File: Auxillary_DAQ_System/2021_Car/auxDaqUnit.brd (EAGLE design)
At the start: 130.8 x 114 mm, 39 parts, among them IC1 ADS1119IPWT, IC2 TPS563231DRLR, J1 1990083, J10 1990083, J11 1990083, J12 1990083, J2 1990083, J3 1990083, J4 1990083, J5 1990083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

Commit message: updated schematic and pinout
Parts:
- added C8: 0.1uF, SparkFun-Capacitors:0603
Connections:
- net 14: now also J10.1; no longer J7.8
- net 15: now also J7.1; no longer J10.8
- net 32: now also J7.8; no longer J10.1
- net 33: now also J10.8; no longer J7.1
- net 5V: now also C8.1, IC1.9
- net GND: now also C8.2, IC2.3; no longer IC1.9
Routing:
- net 15: track 269.2 -> 196.0 mm
- net 33: track 146.2 -> 188.5 mm
- net 14: track 214.0 -> 253.9 mm
- net 32: track 145.1 -> 153.7 mm
- net 5V: track 163.6 -> 167.1 mm
- net 17: track 250.9 -> 252.3 mm
- net 16: track 248.9 -> 250.0 mm
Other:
- board text added: "20"
- board text added: "21"

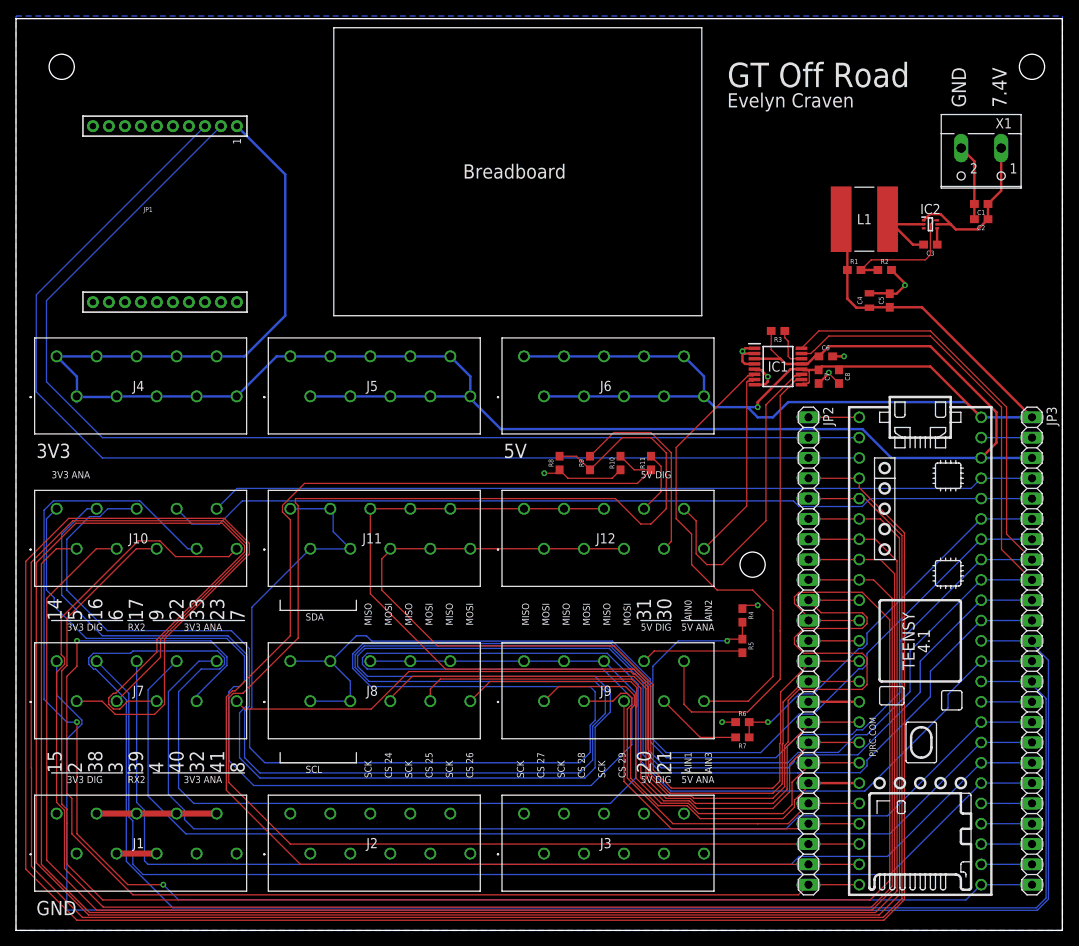
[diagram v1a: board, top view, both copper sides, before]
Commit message: Fixed minor airwires
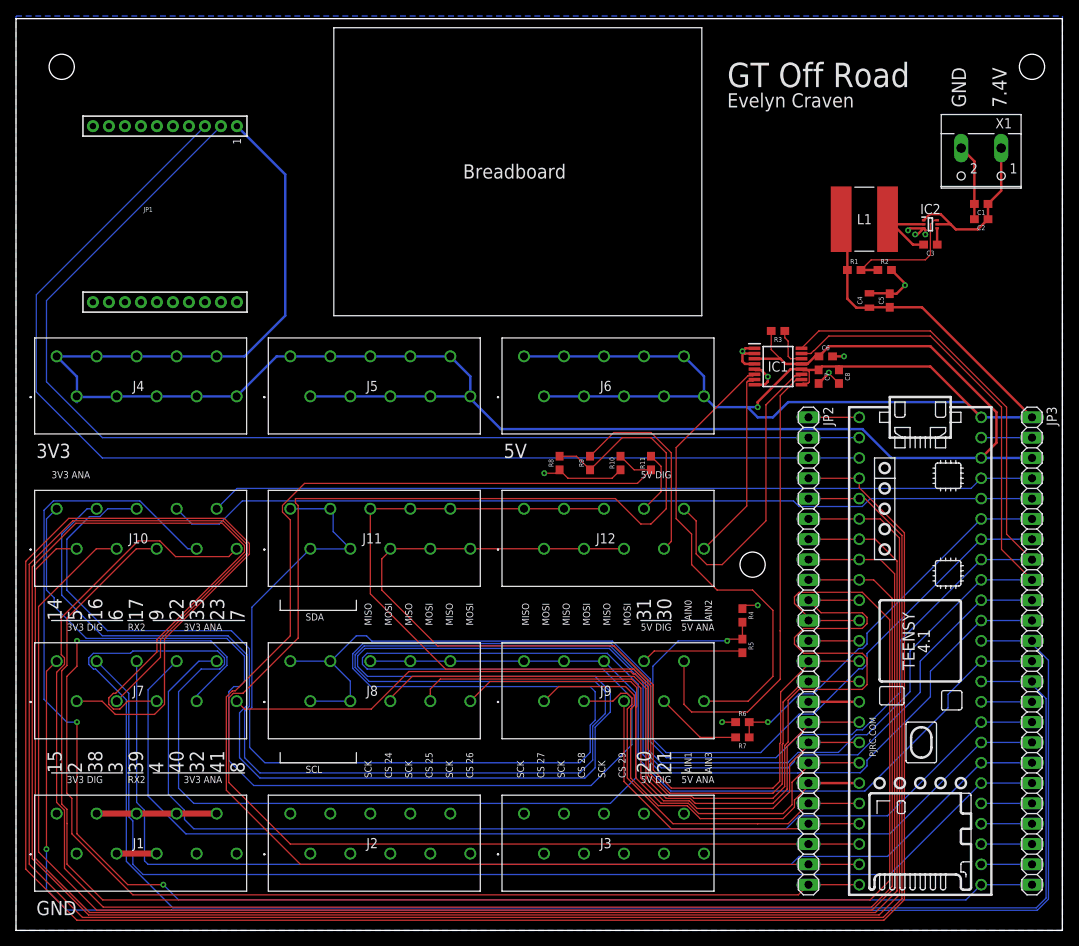
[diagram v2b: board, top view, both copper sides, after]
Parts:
- removed FRAME1: FRAME-LETTER, SparkFun-Aesthetics:CREATIVE_COMMONS
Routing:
- net GND: track 73.8 -> 78.1 mm, vias 8 -> 11
- net 6: track 204.5 -> 205.3 mm
- net 5: track 206.8 -> 207.4 mm
- net 15: track 196.0 -> 195.5 mm, vias 0 -> 1
